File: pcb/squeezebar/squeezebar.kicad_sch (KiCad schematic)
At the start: 37 parts

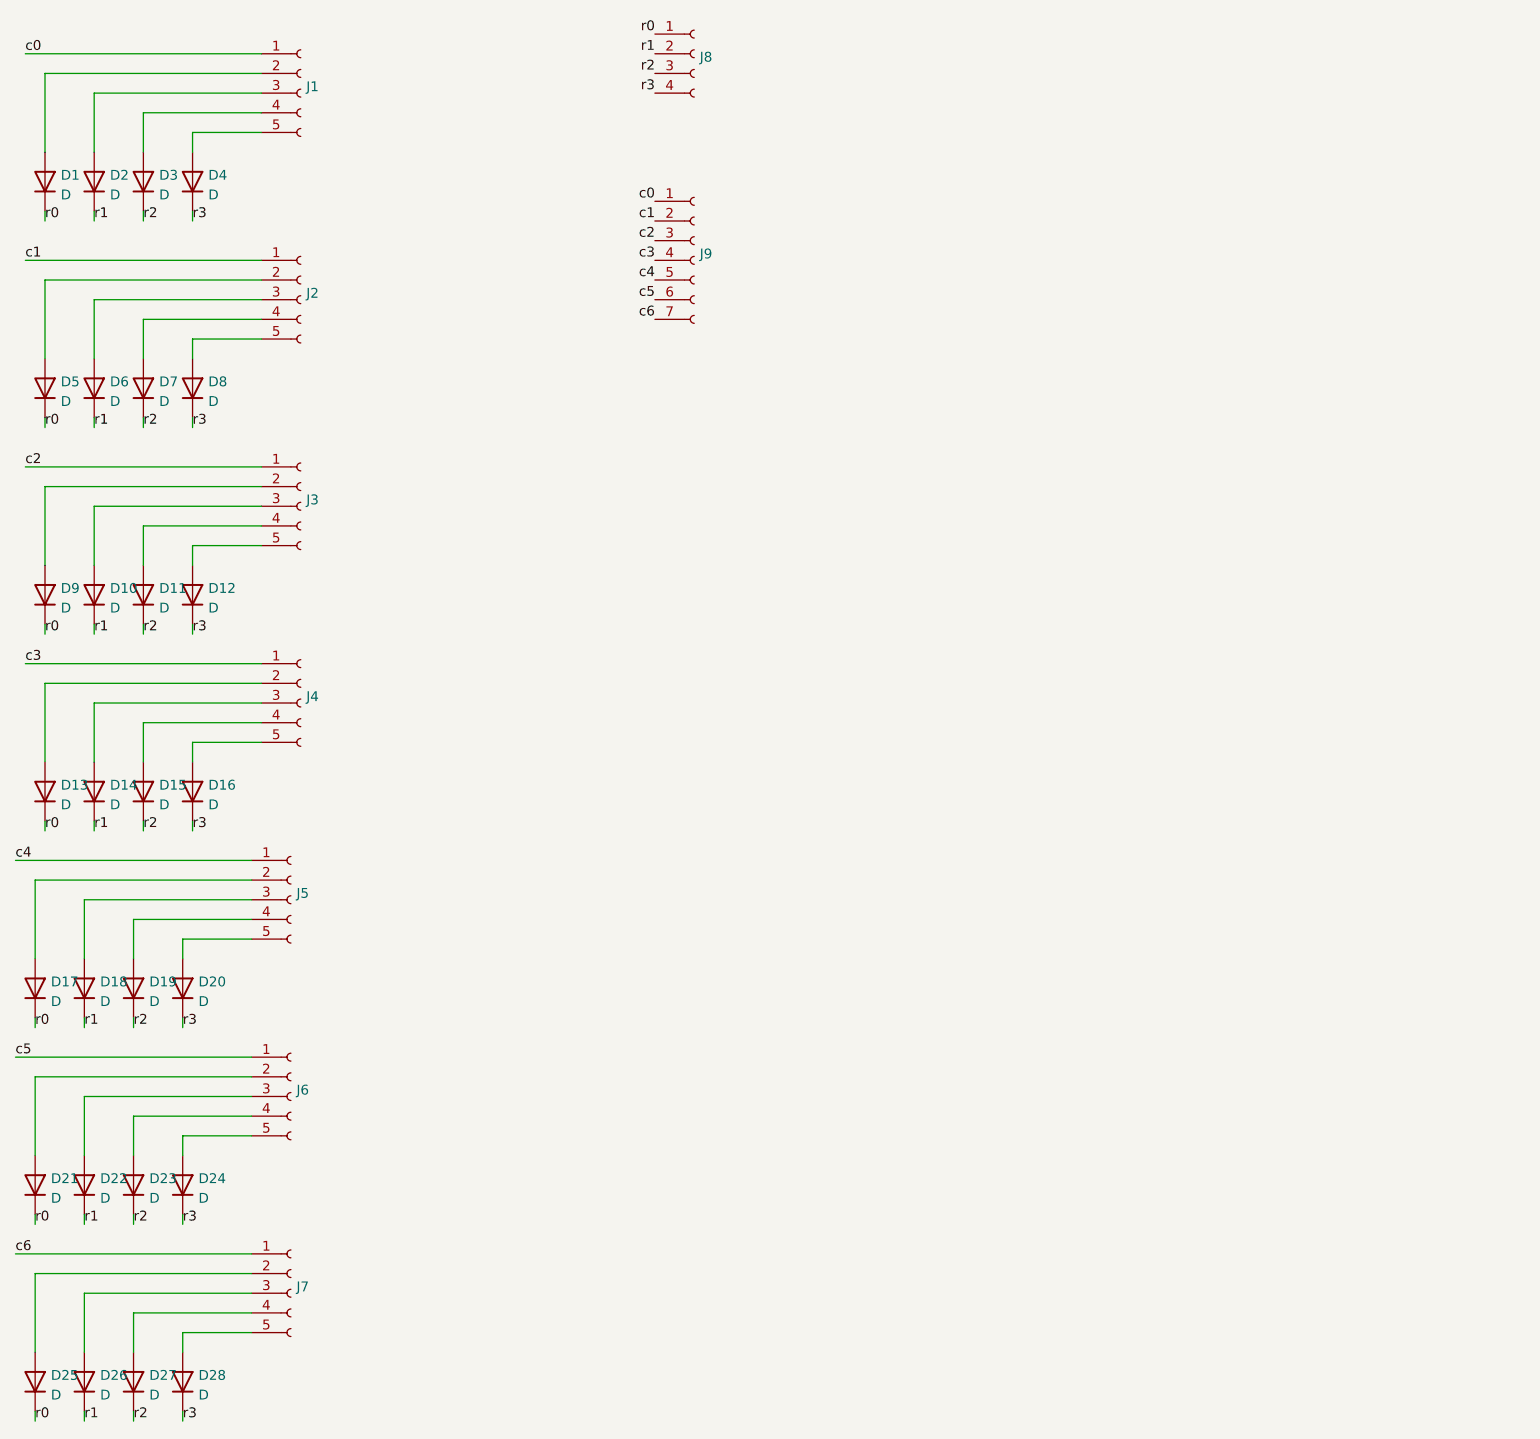
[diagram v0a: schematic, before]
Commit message: Add mounting holes & extra side connectors
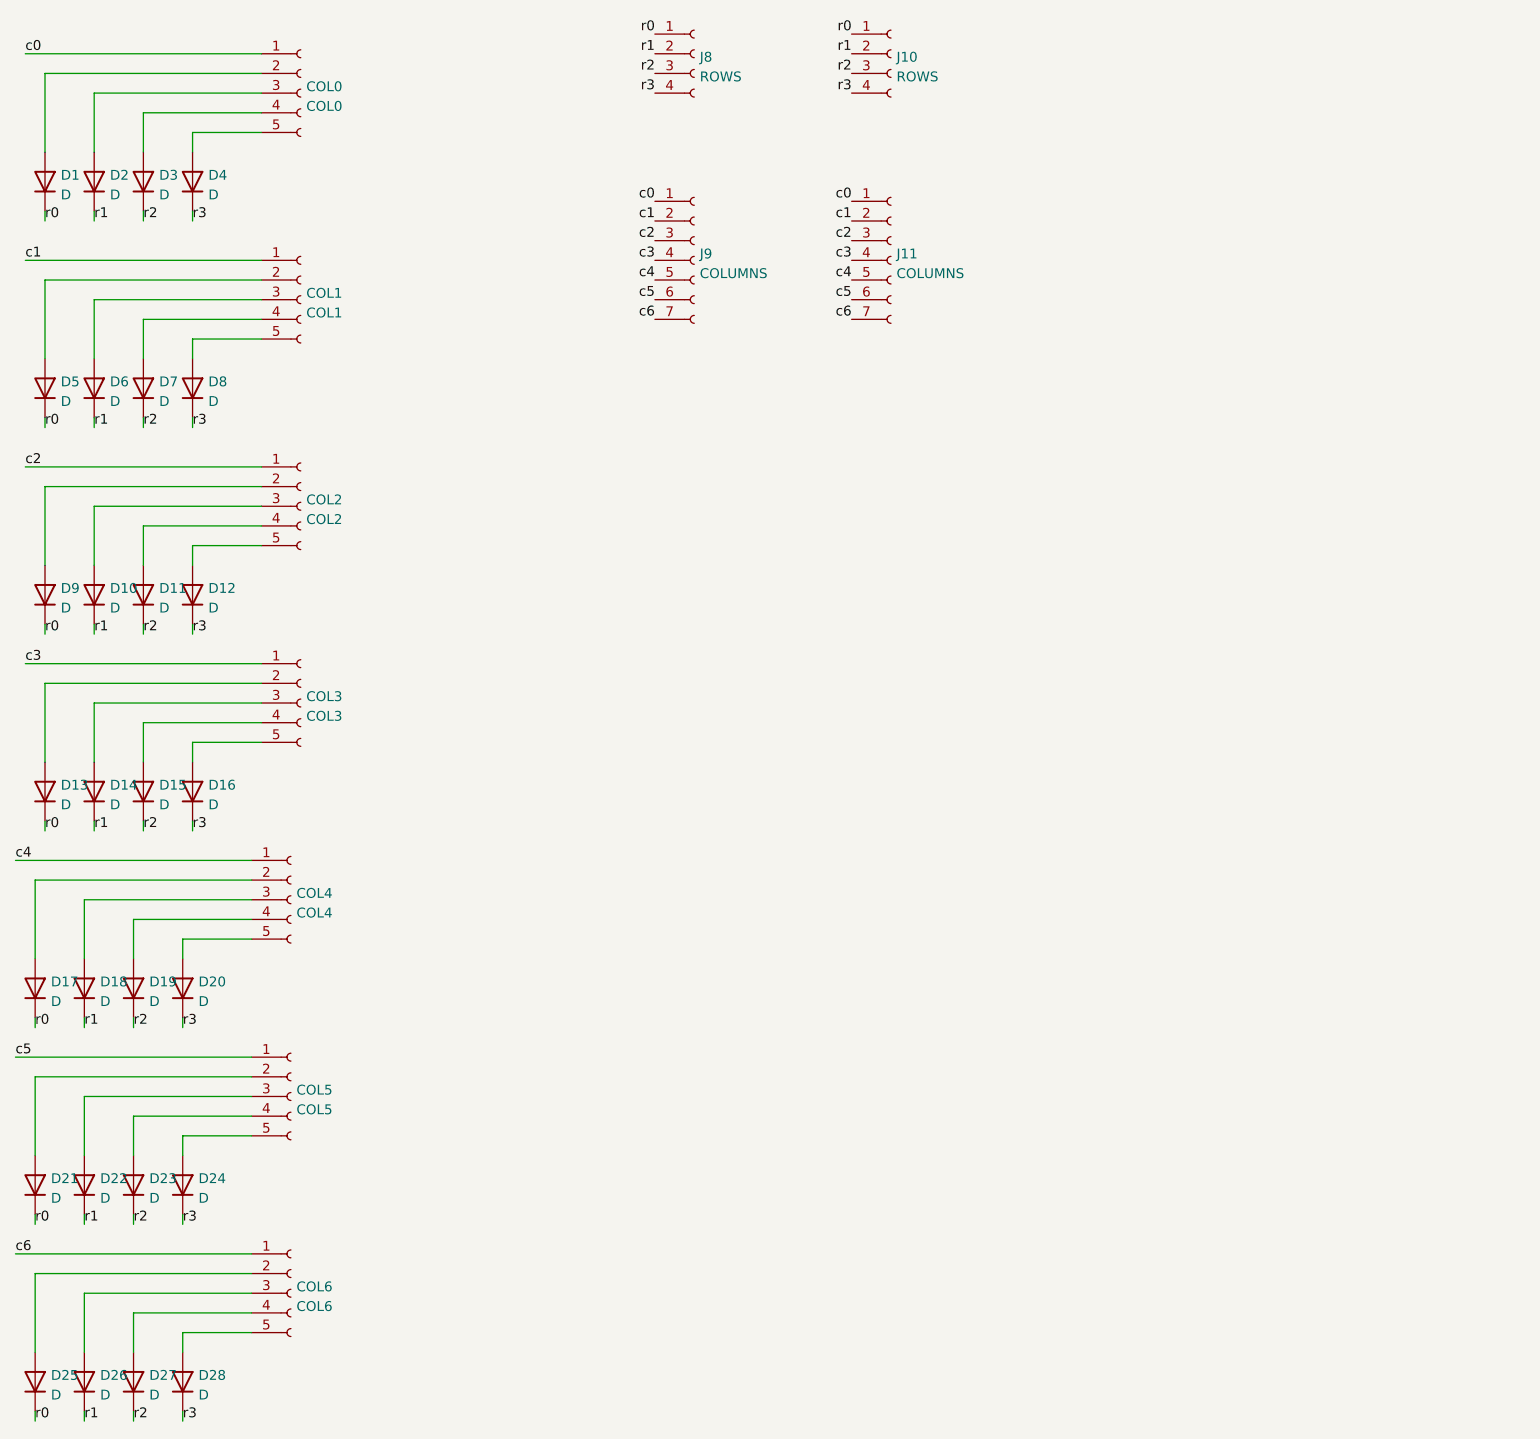
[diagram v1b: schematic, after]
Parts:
- added J10: ROWS, Connector_PinSocket_2.54mm:PinSocket_1x04_P2.54mm_Vertical, symbol Connector:Conn_01x04_Female
- added J11: COLUMNS, Connector_PinSocket_2.54mm:PinSocket_1x07_P2.54mm_Vertical, symbol Connector:Conn_01x07_Female
- COL0: renamed from J1; value (none) -> COL0
- COL1: renamed from J2; value (none) -> COL1
- COL2: renamed from J3; value (none) -> COL2
- COL3: renamed from J4; value (none) -> COL3
- COL4: renamed from J5; value (none) -> COL4
- COL5: renamed from J6; value (none) -> COL5
- COL6: renamed from J7; value (none) -> COL6; footprint Connector_PinHeader_2.54mm:PinHeader_1x05_P2.54mm_Vertical -> (none)
- J8: value (none) -> ROWS; footprint (none) -> Connector_PinSocket_2.54mm:PinSocket_1x04_P2.54mm_Vertical
- J9: value (none) -> COLUMNS; footprint (none) -> Connector_PinSocket_2.54mm:PinSocket_1x07_P2.54mm_Vertical
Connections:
- net c0: now also J11.1 (Pin_1)
- net c1: now also J11.2 (Pin_2)
- net c2: now also J11.3 (Pin_3)
- net c3: now also J11.4 (Pin_4)
- net c4: now also J11.5 (Pin_5)
- net c5: now also J11.6 (Pin_6)
- net c6: now also J11.7 (Pin_7)
- net r0: now also J10.1 (Pin_1)
- net r1: now also J10.2 (Pin_2)
- net r2: now also J10.3 (Pin_3)
- net r3: now also J10.4 (Pin_4)

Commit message: squeezebar: Switch to a more regular layout (WIP)
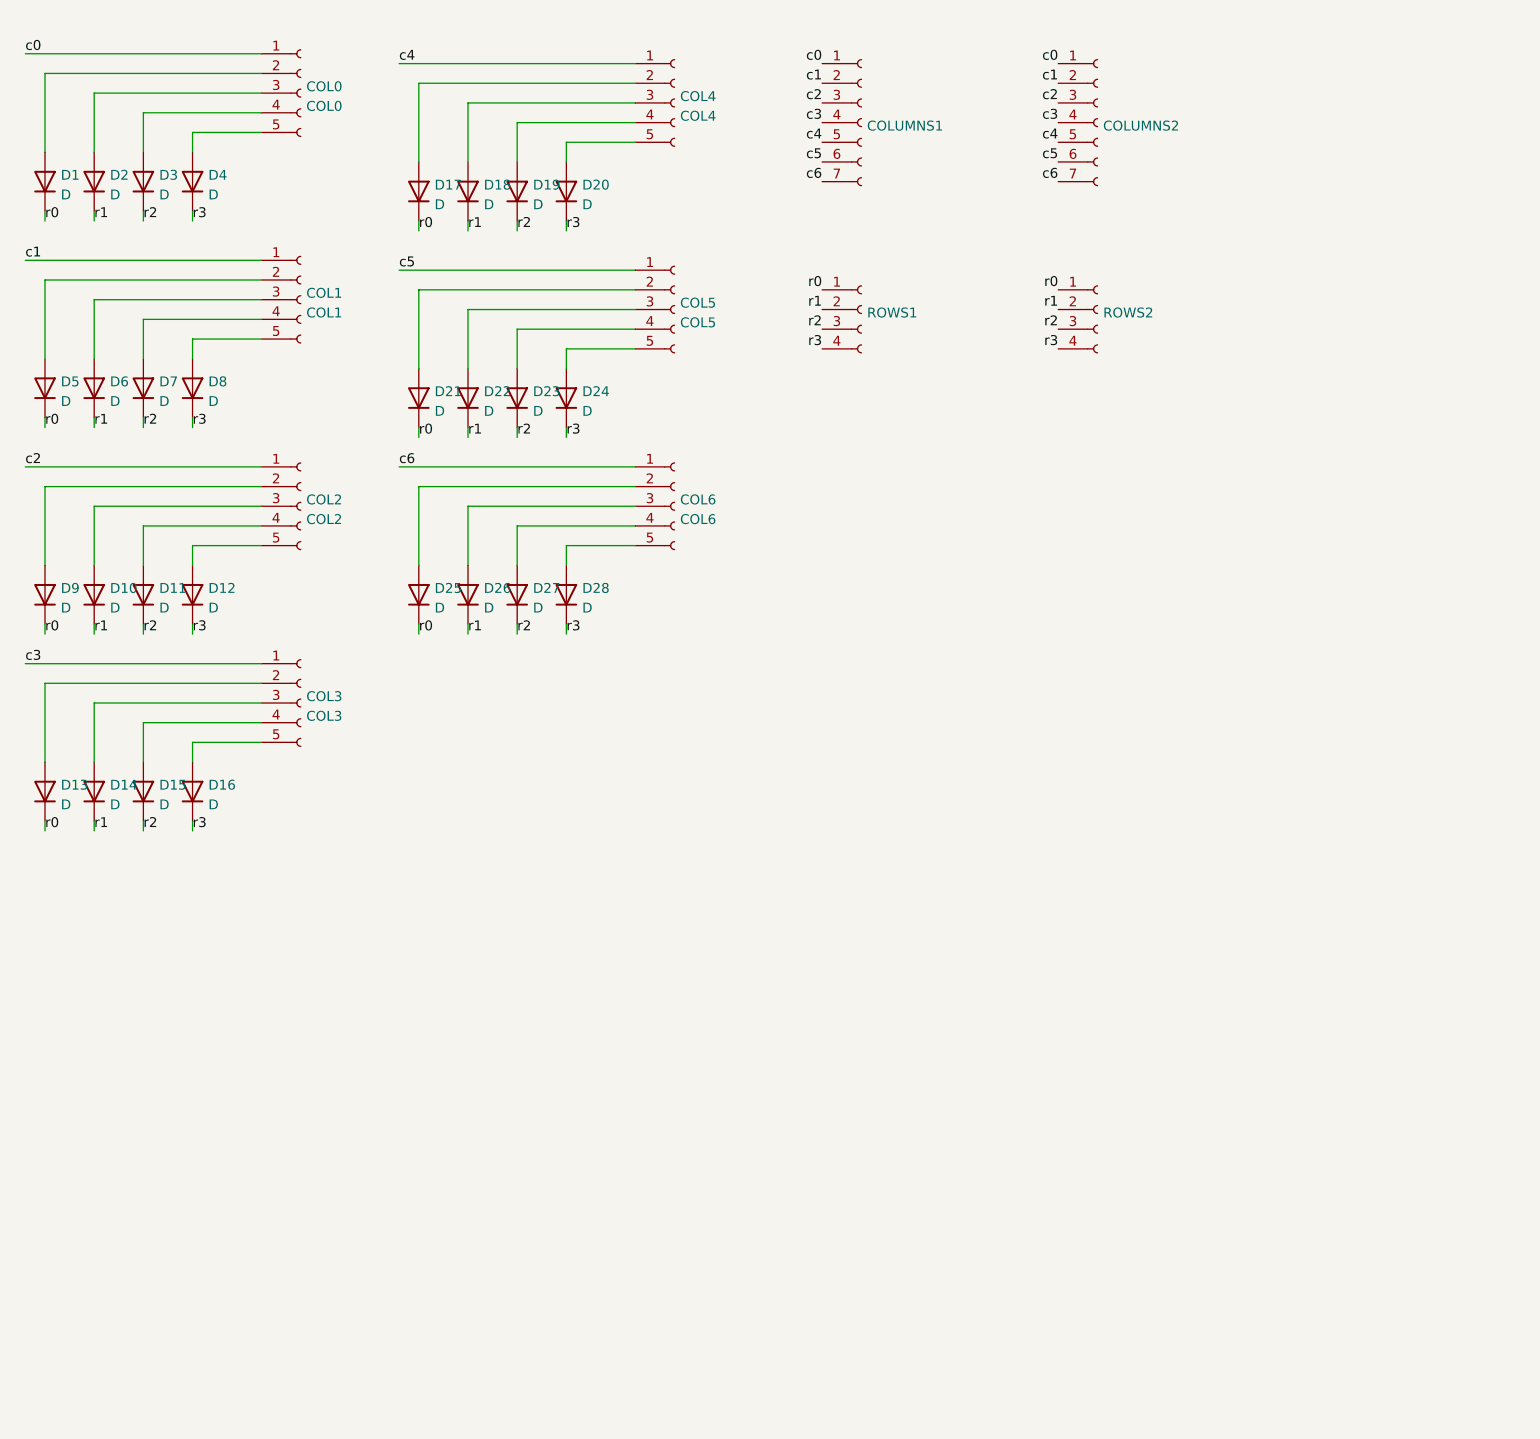
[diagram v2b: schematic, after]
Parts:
- removed J10, J8: ROWS, Connector_PinSocket_2.54mm:PinSocket_1x04_P2.54mm_Vertical, symbol Connector:Conn_01x04_Female
- removed J11, J9: COLUMNS, Connector_PinSocket_2.54mm:PinSocket_1x07_P2.54mm_Vertical, symbol Connector:Conn_01x07_Female
- added COLUMNS1, COLUMNS2: (no value), symbol Connector:Conn_01x07_Female
- added ROWS1, ROWS2: (no value), symbol Connector:Conn_01x04_Female
- COL0, COL1, COL2, COL3, COL4, COL5, COL6: footprint (none) -> Library:PinHeader_1x05_P2.54mm_Vertical
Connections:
- net c0: now also COLUMNS1.1 (Pin_1), COLUMNS2.1 (Pin_1)
- net c1: now also COLUMNS1.2 (Pin_2), COLUMNS2.2 (Pin_2)
- net c2: now also COLUMNS1.3 (Pin_3), COLUMNS2.3 (Pin_3)
- net c3: now also COLUMNS1.4 (Pin_4), COLUMNS2.4 (Pin_4)
- net c4: now also COLUMNS1.5 (Pin_5), COLUMNS2.5 (Pin_5)
- net c5: now also COLUMNS1.6 (Pin_6), COLUMNS2.6 (Pin_6)
- net c6: now also COLUMNS1.7 (Pin_7), COLUMNS2.7 (Pin_7)
- net r0: now also ROWS1.1 (Pin_1), ROWS2.1 (Pin_1)
- net r1: now also ROWS1.2 (Pin_2), ROWS2.2 (Pin_2)
- net r2: now also ROWS1.3 (Pin_3), ROWS2.3 (Pin_3)
- net r3: now also ROWS1.4 (Pin_4), ROWS2.4 (Pin_4)
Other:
- moved on the sheet: COL4, COL5, COL6, D17, D18, D19, D20, D21, D22, D23, D24, D25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

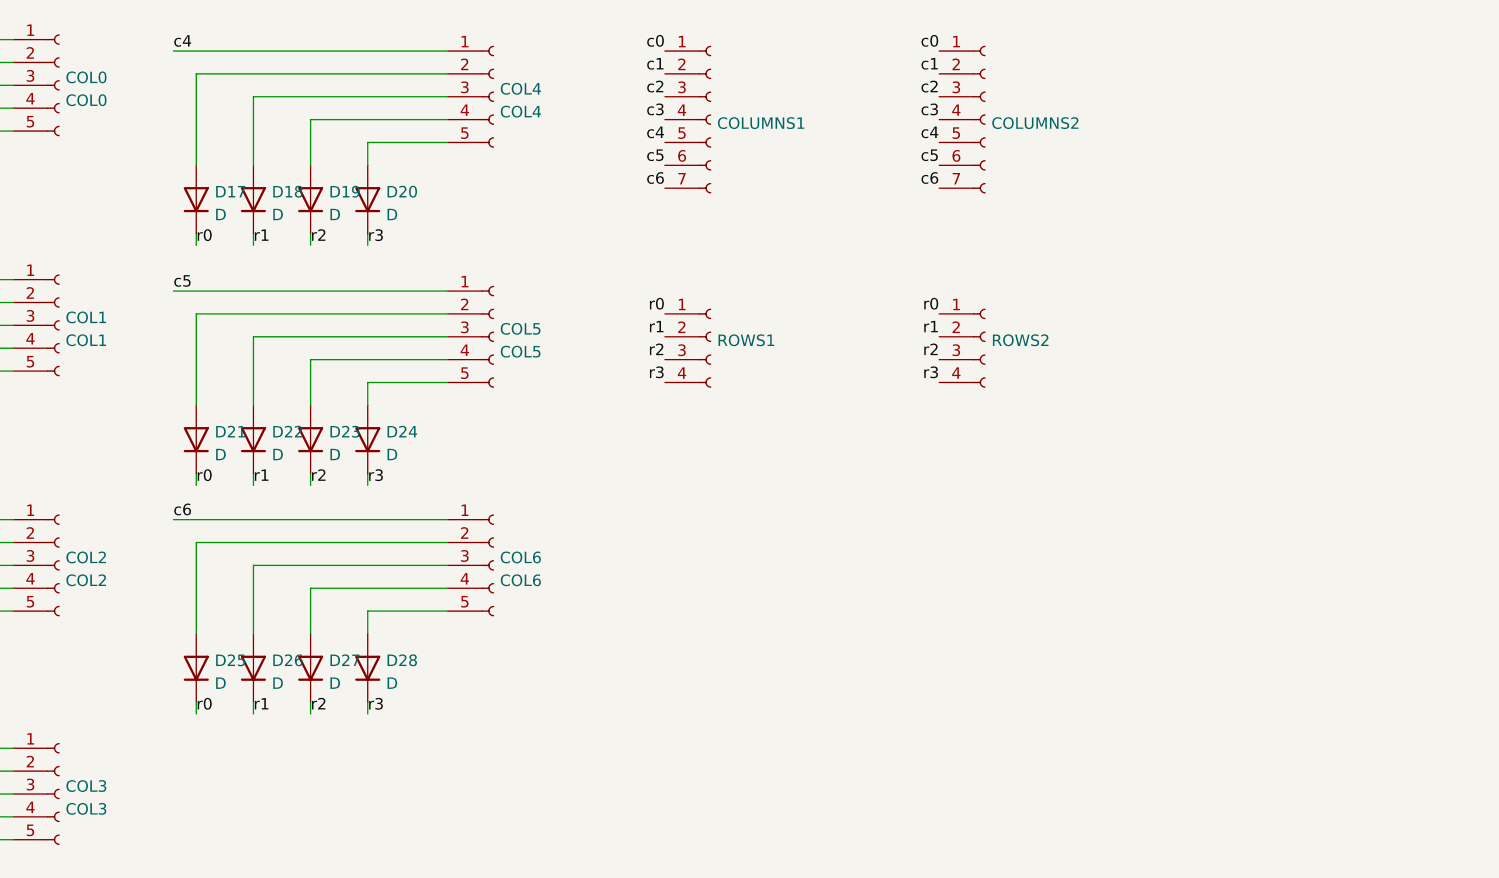
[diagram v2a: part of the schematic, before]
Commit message: Squeezebar: New layout
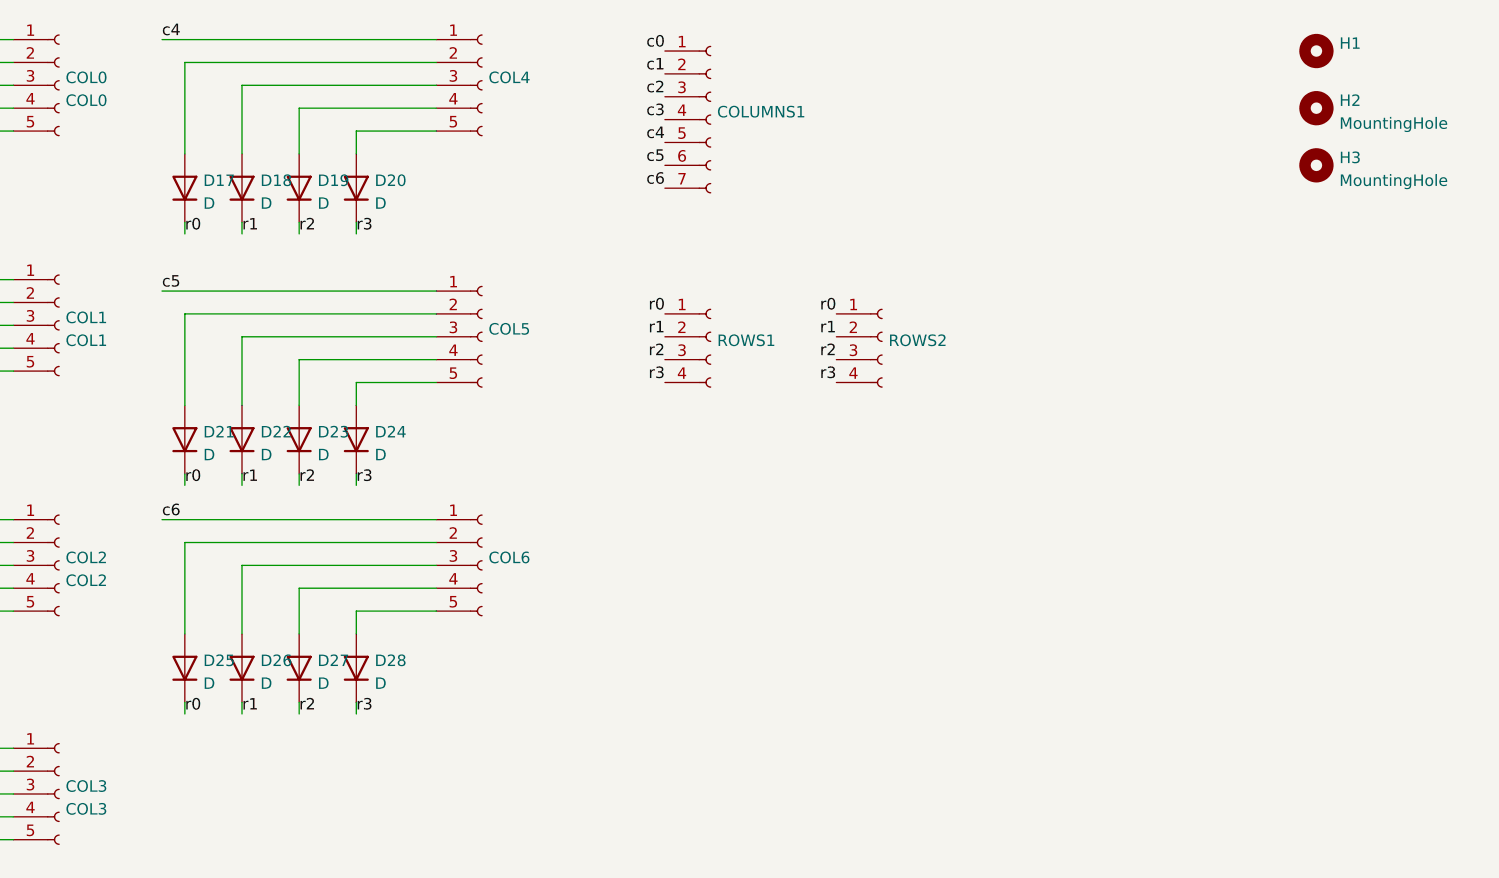
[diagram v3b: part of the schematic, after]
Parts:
- removed COLUMNS2: (no value), symbol Connector:Conn_01x07_Female
- added H1: (no value), symbol Mechanical:MountingHole
- added H2: MountingHole, symbol Mechanical:MountingHole
- added H3: MountingHole, MountingHole:MountingHole_2.2mm_M2_DIN965, symbol Mechanical:MountingHole
- COL4: value COL4 -> (none)
- COL5: value COL5 -> (none)
- COL6: value COL6 -> (none)
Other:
- moved on the sheet: ROWS2
